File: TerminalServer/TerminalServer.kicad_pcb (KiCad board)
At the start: 4 copper layers, 135 x 72 mm, 128 parts, among them J1 RJ45_LED, J10 Conn_01x10_Pin, J11 SI-60118-F, J12 Conn_01x08_Pin, J13 503398-1892, J2 RJ45_LED, J3 RJ45_LED, J4 RJ45_LED, J5 RJ45_LED, J6 RJ45_LED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

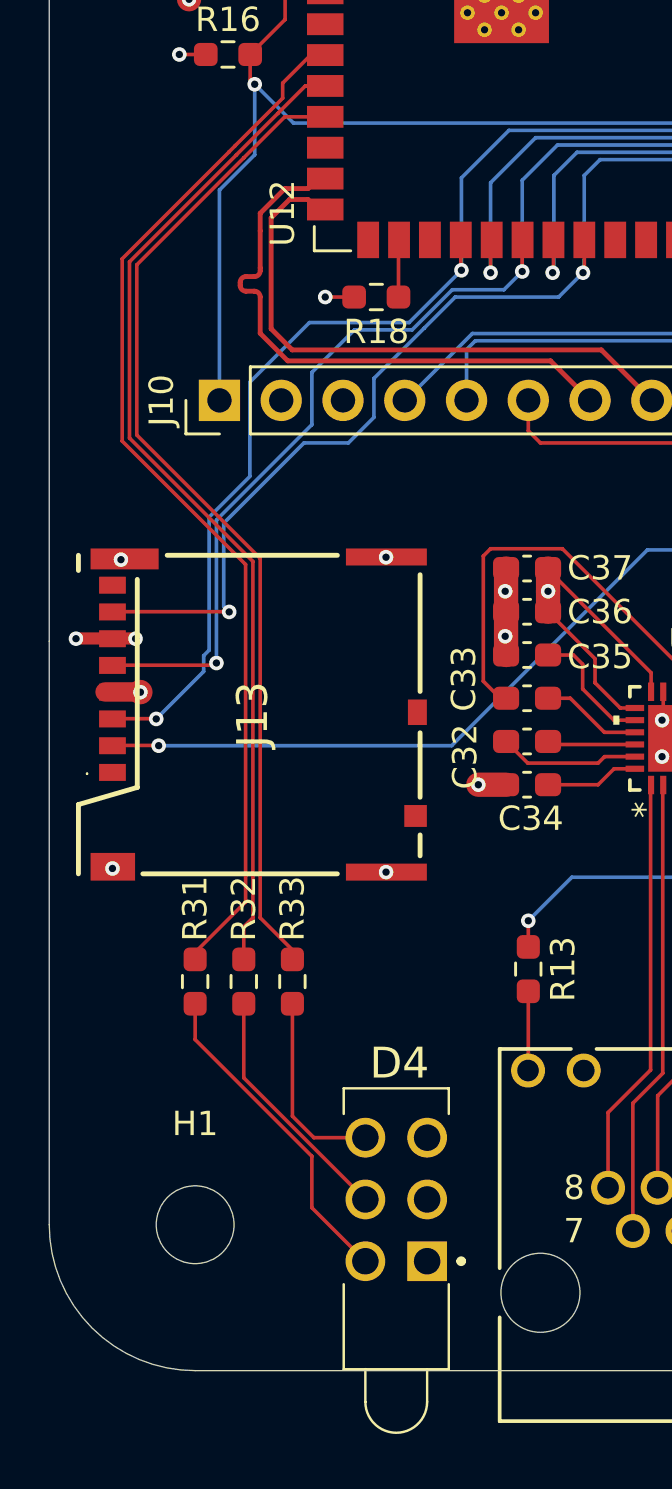
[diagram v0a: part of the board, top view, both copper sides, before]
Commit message: Reverted to quad LED
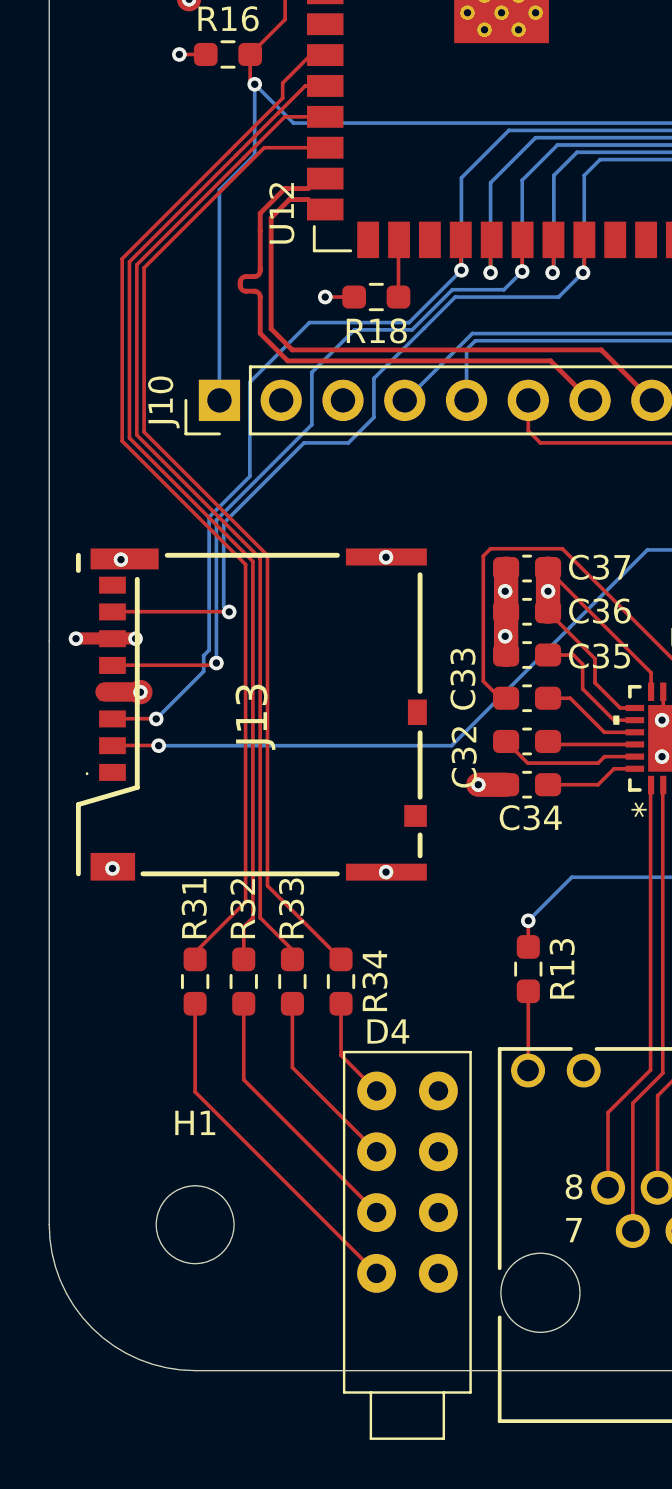
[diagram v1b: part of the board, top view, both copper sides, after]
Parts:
- added R34: 100R, Resistor_SMD:R_0603_1608Metric_Pad0.98x0.95mm_HandSolder, F.Cu at (83.0, 120.0)
- D4: value 564-0100-132F -> Green; footprint Triple LED:5640100222F -> XINGLIGHT:XL-DZ234SYGD-4
- moved D4 1.79 mm to (85.7, 129.9)
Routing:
- net /LED4: track 0.00 -> 41.3 mm
- net Net-(D4-LED_A4): track 0.00 -> 4.19 mm
- net Net-(D4-LED_A1): track 13.5 -> 14.2 mm
